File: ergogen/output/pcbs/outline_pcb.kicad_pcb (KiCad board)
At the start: 2 copper layers, 153.9 x 127.4 mm, 0 parts

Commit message: final key layout
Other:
- board size 153.9 x 127.4 mm -> 150.7 x 117.3 mm
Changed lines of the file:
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@@
     (add_net "")
   )
-  (gr_line (start 88.475 106.525) (end 88.475 71.5460678) (angle 90) (layer Edge.Cuts) (width 0.15))
-(gr_line (start 89.93946609999999 68.0105339) (end 106.64037364705325 51.30962635294672) (angle 90) (layer Edge.Cuts) (width 0.15))
-(gr_line (start 108.59476856705334 50.10174381294672) (end 144.7052493281026 38.06491685999999) (angle 90) (layer Edge.Cuts) (width 0.15))
+  (gr_line (start 88.475 106.525) (end 88.475 55.475) (angle 90) (layer Edge.Cuts) (width 0.15))
+(gr_line (start 93.475 50.475) (end 106.6636117040513 50.475) (angle 90) (layer Edge.Cuts) (width 0.15))
+(gr_line (start 108.24475068405127 50.21841644000001) (end 144.7052493281026 38.06491685999999) (angle 90) (layer Edge.Cuts) (width 0.15))
 (gr_line (start 146.28638830810263 37.808333299999994) (end 167.71361169189737 37.808333299999994) (angle 90) (layer Edge.Cuts) (width 0.15))
 (gr_line (start 169.29475067189742 38.06491686000001) (end 186.7552493281026 43.88508313999999) (angle 90) (layer Edge.Cuts) (width 0.15))
 (gr_line (start 188.33638830810264 44.14166670000001) (end 201.525 44.14166670000001) (angle 90) (layer Edge.Cuts) (width 0.15))
-(gr_line (start 206.525 49.14166670000001) (end 206.525 102.86029813582074) (angle 90) (layer Edge.Cuts) (width 0.15))
-(gr_line (start 208.310848458677 106.69034118506215) (end 228.85758585017504 123.93305342657186) (angle 90) (layer Edge.Cuts) (width 0.15))
-(gr_line (start 229.95649270366894 125.2337630374966) (end 241.64119033224497 145.15868801627232) (angle 90) (layer Edge.Cuts) (width 0.15))
-(gr_line (start 241.158354054793 150.9019595530699) (end 230.6106260569508 163.47225228109312) (angle 90) (layer Edge.Cuts) (width 0.15))
-(gr_line (start 225.58488799745365 165.1132849476129) (end 209.01584779050745 161.03322954678592) (angle 90) (layer Edge.Cuts) (width 0.15))
-(gr_line (start 208.0121531737926 160.66863440194044) (end 192.12719173750745 152.8888005186954) (angle 90) (layer Edge.Cuts) (width 0.15))
-(gr_line (start 191.63808173419523 152.68071298626947) (end 171.31199179532285 145.28262126982034) (angle 90) (layer Edge.Cuts) (width 0.15))
-(gr_line (start 169.4267896475063 144.0588953137715) (end 139.47299518832543 113.06577151067273) (angle 90) (layer Edge.Cuts) (width 0.15))
-(gr_line (start 135.88042248486482 111.54050940720487) (end 107.4762820473185 111.52500069999994) (angle 90) (layer Edge.Cuts) (width 0.15))
-(gr_line (start 107.4735520474277 111.525) (end 93.475 111.525) (angle 90) (layer Edge.Cuts) (width 0.15))
-(gr_arc (start 93.475 71.5460678) (end 89.93946609999999 68.0105339) (angle -45) (layer Edge.Cuts) (width 0.15))
-(gr_arc (start 110.17590754705328 54.84516025294673) (end 108.59476854705329 50.101743852946726) (angle -26.565049365227154) (layer Edge.Cuts) (width 0.15))
+(gr_line (start 206.525 49.14166670000001) (end 206.525 102.30752500839418) (angle 90) (layer Edge.Cuts) (width 0.15))
+(gr_line (start 209.02161 106.63569300839418) (end 221.75052627511832 113.99803233196393) (angle 90) (layer Edge.Cuts) (width 0.15))
+(gr_line (start 223.0554553331315 115.0863382826102) (end 238.02377626345935 132.6809584733316) (angle 90) (layer Edge.Cuts) (width 0.15))
+(gr_line (start 238.54558420544618 138.4208205226853) (end 230.34090833802992 152.6317360151316) (angle 90) (layer Edge.Cuts) (width 0.15))
+(gr_line (start 225.67648483180594 155.12054810801365) (end 208.65067101680498 153.9796614916567) (angle 90) (layer Edge.Cuts) (width 0.15))
+(gr_line (start 207.59891348870966 153.7948950177248) (end 190.60432732339262 148.89164919504304) (angle 90) (layer Edge.Cuts) (width 0.15))
+(gr_line (start 190.08651425185596 148.77165602506335) (end 169.35856764628346 145.11675977833818) (angle 90) (layer Edge.Cuts) (width 0.15))
+(gr_line (start 166.4937897641463 143.51906585122265) (end 139.4902371365632 113.21409806628387) (angle 90) (layer Edge.Cuts) (width 0.15))
+(gr_line (start 135.75994829153424 111.54044362809798) (end 107.4762820473352 111.52500069999995) (angle 90) (layer Edge.Cuts) (width 0.15))
+(gr_line (start 107.4735520474444 111.525) (end 93.475 111.525) (angle 90) (layer Edge.Cuts) (width 0.15))
+(gr_arc (start 93.475 55.475) (end 93.475 50.475) (angle -90) (layer Edge.Cuts) (width 0.15))
+(gr_arc (start 106.6636117040513 45.475) (end 106.6636117040513 50.475) (angle -18.43495063477326) (layer Edge.Cuts) (width 0.15))
 (gr_arc (start 146.28638830810263 42.80833329999999) (end 146.28638830810263 37.80833329999999) (angle -18.43495063477387) (layer Edge.Cuts) (width 0.15))
 (gr_arc (start 167.71361169189737 42.808333299999994) (end 169.29475069189738 38.06491689999999) (angle -18.43495063477424) (layer Edge.Cuts) (width 0.15))
 (gr_arc (start 188.33638830810264 39.14166670000001) (end 186.75524930810263 43.88508310000001) (angle -18.434950634774225) (layer Edge.Cuts) (width 0.15))
 (gr_arc (start 201.525 49.14166670000001) (end 206.525 49.14166670000001) (angle -90) (layer Edge.Cuts) (width 0.15))
-(gr_arc (start 211.525 102.86029813582074) (end 206.525 102.86029813582074) (angle -49.99680620771349) (layer Edge.Cuts) (width 0.15))
-(gr_arc (start 225.64343430885205 127.7630964758133) (end 229.95649270885204 125.2337630758133) (angle -19.607904513324968) (layer Edge.Cuts) (width 0.15))
-(gr_arc (start 237.3281319374281 147.68802145458915) (end 241.15835413742812 150.90195955458915) (angle -70.38890285726625) (layer Edge.Cuts) (width 0.15))
-(gr_arc (start 226.78040393958594 160.25831418261237) (end 225.58488793958594 165.11328498261236) (angle -63.83361485265897) (layer Edge.Cuts) (width 0.15))
-(gr_arc (start 210.21136373263977 156.1782587817854) (end 208.01215323263978 160.66863438178538) (angle -12.260191503351336) (layer Edge.Cuts) (width 0.15))
-(gr_arc (start 189.92798117866025 157.37917613885043) (end 192.12719167866024 152.88880053885043) (angle -6.093809444231724) (layer Edge.Cuts) (width 0.15))
-(gr_arc (start 173.02209235085783 140.58415811723938) (end 169.42678965085784 144.05889531723938) (angle -25.976973101265287) (layer Edge.Cuts) (width 0.15))
-(gr_arc (start 135.87769248497395 116.54050870720494) (end 139.47299518497394 113.06577150720494) (angle -45.945687680284905) (layer Edge.Cuts) (width 0.15))
-(gr_arc (start 107.4735520474277 116.525) (end 107.4762820474277 111.5250007) (angle -0.03128349563384347) (layer Edge.Cuts) (width 0.15))
+(gr_arc (start 211.525 102.30752500839418) (end 206.525 102.30752500839418) (angle -59.955133554349544) (layer Edge.Cuts) (width 0.15))
+(gr_arc (start 219.24713627511832 118.32620033196392) (end 223.05545527511833 115.08633833196392) (angle -19.566229562522317) (layer Edge.Cuts) (width 0.15))
+(gr_arc (start 234.21545720544614 135.9208205226853) (end 238.54558420544615 138.4208205226853) (angle -70.38890410024266) (layer Edge.Cuts) (width 0.15))
+(gr_arc (start 226.01078133802991 150.13173601513165) (end 225.67648483802992 155.12054811513164) (angle -63.833615430284226) (layer Edge.Cuts) (width 0.15))
+(gr_arc (start 208.98496752302896 148.99084939877474) (end 207.59891352302895 153.79489499877474) (angle -12.26019167495545) (layer Edge.Cuts) (width 0.15))
+(gr_arc (start 189.21827328907335 153.6956948139931) (end 190.60432728907335 148.8916492139931) (angle -6.093806421000238) (layer Edge.Cuts) (width 0.15))
+(gr_arc (start 170.2268086090661 140.19272098940846) (end 166.4937897090661 143.51906588940847) (angle -38.29703551275779) (layer Edge.Cuts) (width 0.15))
+(gr_arc (start 135.75721829164337 116.54044292809806) (end 139.49023719164336 113.21409802809806) (angle -48.26575280977835) (layer Edge.Cuts) (width 0.15))
+(gr_arc (start 107.4735520474444 116.525) (end 107.4762820474444 111.5250007) (angle -0.03128349563384347) (layer Edge.Cuts) (width 0.15))
 (gr_arc (start 93.475 106.525) (end 88.475 106.525) (angle -90) (layer Edge.Cuts) (width 0.15))
 )

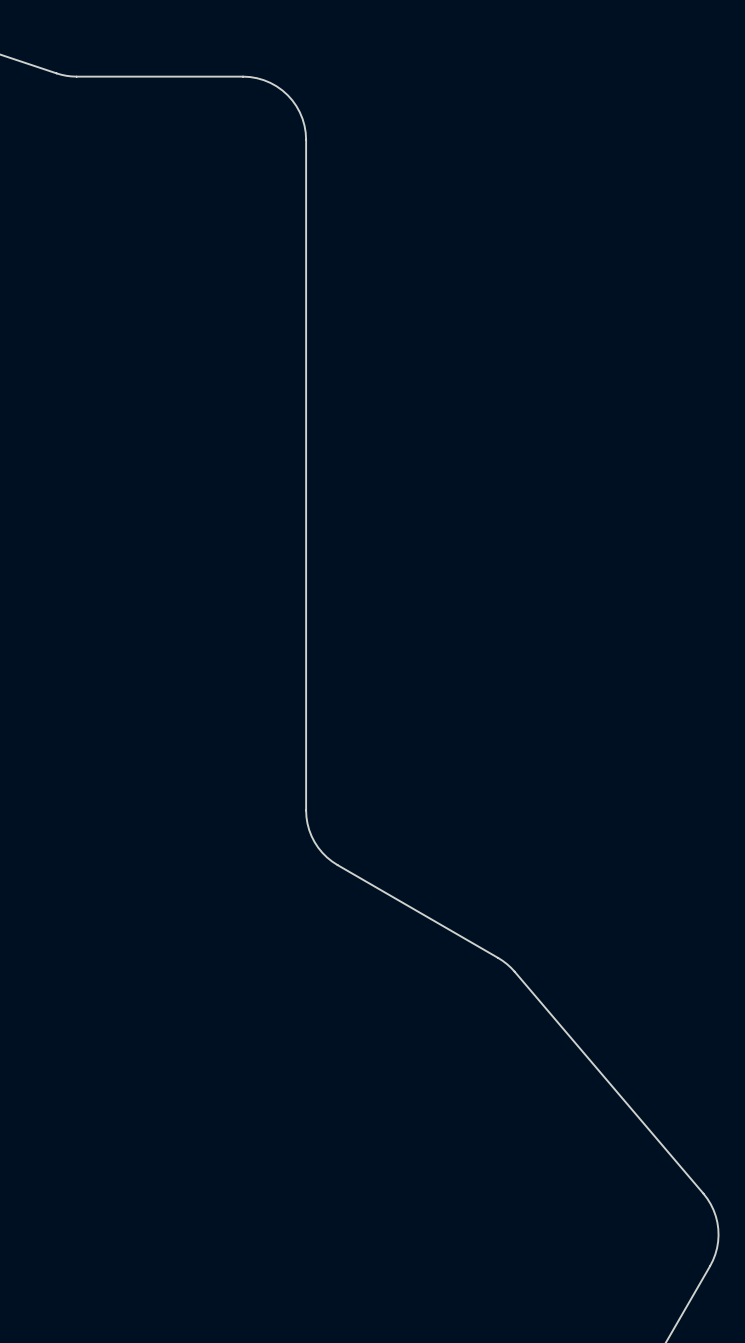
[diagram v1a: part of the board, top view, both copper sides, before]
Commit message: fix pcb (update sw footprint), start case design
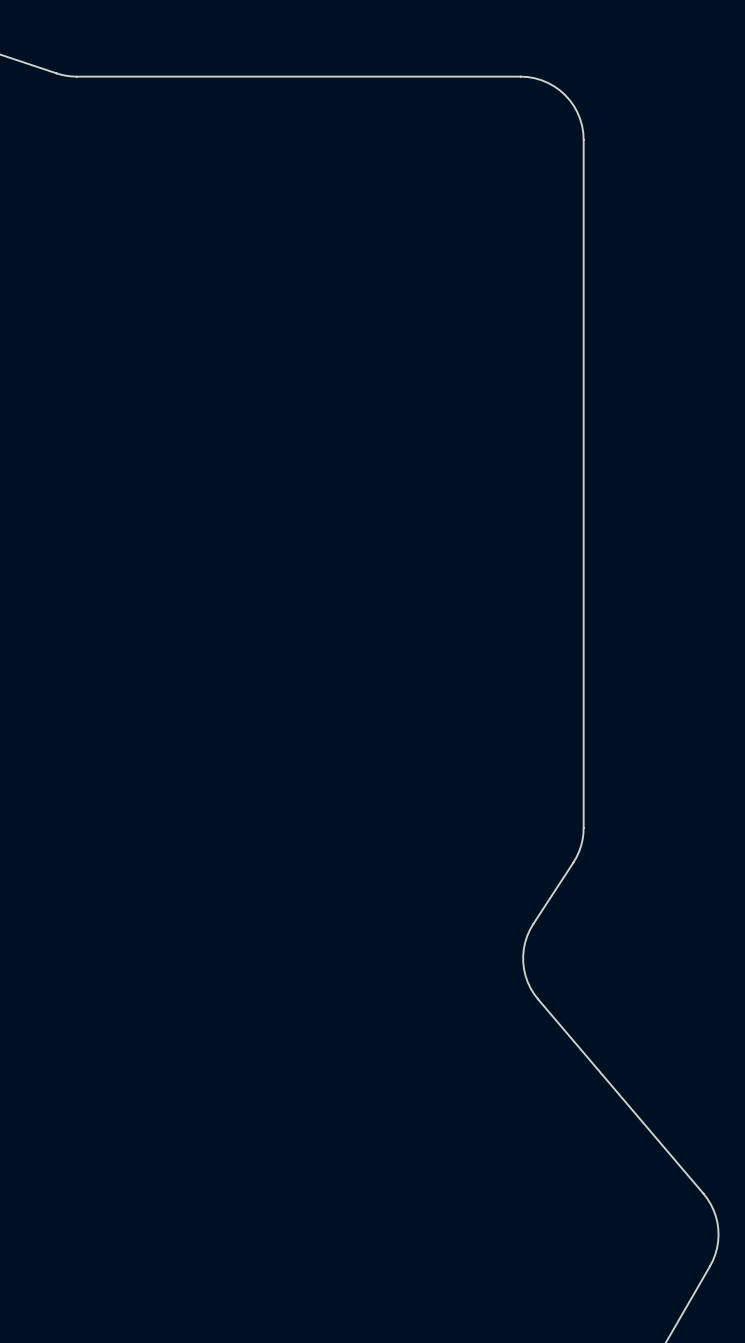
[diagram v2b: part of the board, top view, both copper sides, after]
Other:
- outline, holes or cut-outs redrawn
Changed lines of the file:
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@@
 (gr_line (start 146.28638830810263 37.808333299999994) (end 167.71361169189737 37.808333299999994) (angle 90) (layer Edge.Cuts) (width 0.15))
 (gr_line (start 169.29475067189742 38.06491686000001) (end 186.7552493281026 43.88508313999999) (angle 90) (layer Edge.Cuts) (width 0.15))
-(gr_line (start 188.33638830810264 44.14166670000001) (end 201.525 44.14166670000001) (angle 90) (layer Edge.Cuts) (width 0.15))
-(gr_line (start 206.525 49.14166670000001) (end 206.525 102.30752500839418) (angle 90) (layer Edge.Cuts) (width 0.15))
-(gr_line (start 209.02161 106.63569300839418) (end 221.75052627511832 113.99803233196393) (angle 90) (layer Edge.Cuts) (width 0.15))
-(gr_line (start 223.0554553331315 115.0863382826102) (end 238.02377626345935 132.6809584733316) (angle 90) (layer Edge.Cuts) (width 0.15))
+(gr_line (start 188.33638830810264 44.14166670000001) (end 223.525 44.14166670000001) (angle 90) (layer Edge.Cuts) (width 0.15))
+(gr_line (start 228.525 49.14166670000001) (end 228.525 103.7046128906315) (angle 90) (layer Edge.Cuts) (width 0.15))
+(gr_line (start 227.71235002139701 106.43702940459406) (end 224.53776635689925 111.30198750768221) (angle 90) (layer Edge.Cuts) (width 0.15))
+(gr_line (start 224.91679732028317 117.27426607099835) (end 238.02377626345938 132.68095847333166) (angle 90) (layer Edge.Cuts) (width 0.15))
 (gr_line (start 238.54558420544618 138.4208205226853) (end 230.34090833802992 152.6317360151316) (angle 90) (layer Edge.Cuts) (width 0.15))
 (gr_line (start 225.67648483180594 155.12054810801365) (end 208.65067101680498 153.9796614916567) (angle 90) (layer Edge.Cuts) (width 0.15))
@@
 (gr_arc (start 167.71361169189737 42.808333299999994) (end 169.29475069189738 38.06491689999999) (angle -18.43495063477424) (layer Edge.Cuts) (width 0.15))
 (gr_arc (start 188.33638830810264 39.14166670000001) (end 186.75524930810263 43.88508310000001) (angle -18.434950634774225) (layer Edge.Cuts) (width 0.15))
-(gr_arc (start 201.525 49.14166670000001) (end 206.525 49.14166670000001) (angle -90) (layer Edge.Cuts) (width 0.15))
-(gr_arc (start 211.525 102.30752500839418) (end 206.525 102.30752500839418) (angle -59.955133554349544) (layer Edge.Cuts) (width 0.15))
-(gr_arc (start 219.24713627511832 118.32620033196392) (end 223.05545527511833 115.08633833196392) (angle -19.566229562522317) (layer Edge.Cuts) (width 0.15))
-(gr_arc (start 234.21545720544614 135.9208205226853) (end 238.54558420544615 138.4208205226853) (angle -70.38890410024266) (layer Edge.Cuts) (width 0.15))
+(gr_arc (start 223.525 49.14166670000001) (end 228.525 49.14166670000001) (angle -90) (layer Edge.Cuts) (width 0.15))
+(gr_arc (start 223.525 103.7046128906315) (end 227.71235000000001 106.4370293906315) (angle -33.12608559132428) (layer Edge.Cuts) (width 0.15))
+(gr_arc (start 228.72511637829635 114.03440402164466) (end 224.53776637829634 111.30198752164466) (angle -73.51498958314954) (layer Edge.Cuts) (width 0.15))
+(gr_arc (start 234.21545720544617 135.9208205226853) (end 238.54558420544618 138.4208205226853) (angle -70.3889041002424) (layer Edge.Cuts) (width 0.15))
 (gr_arc (start 226.01078133802991 150.13173601513165) (end 225.67648483802992 155.12054811513164) (angle -63.833615430284226) (layer Edge.Cuts) (width 0.15))
 (gr_arc (start 208.98496752302896 148.99084939877474) (end 207.59891352302895 153.79489499877474) (angle -12.26019167495545) (layer Edge.Cuts) (width 0.15))
